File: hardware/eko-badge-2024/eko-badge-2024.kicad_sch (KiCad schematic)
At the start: 34 parts, among them J1 UART, J2 Battery, J3 Conn_02x03_Odd_Even, J4 OLED, J5 Conn_02x03_Odd_Even, J6 Conn_02x03_Odd_Even, P1 USB_C_Plug_USB2.0, Q1 DMG3415U-7, SW1 ON, SW2 LEFT, SW3 UP, SW4 DOWN, SW5 RESET, SW6 BOOT, SW7 RIGTH, U1 ESP32-C6-WROOM-1-N4, U2 AP2112K-3.3

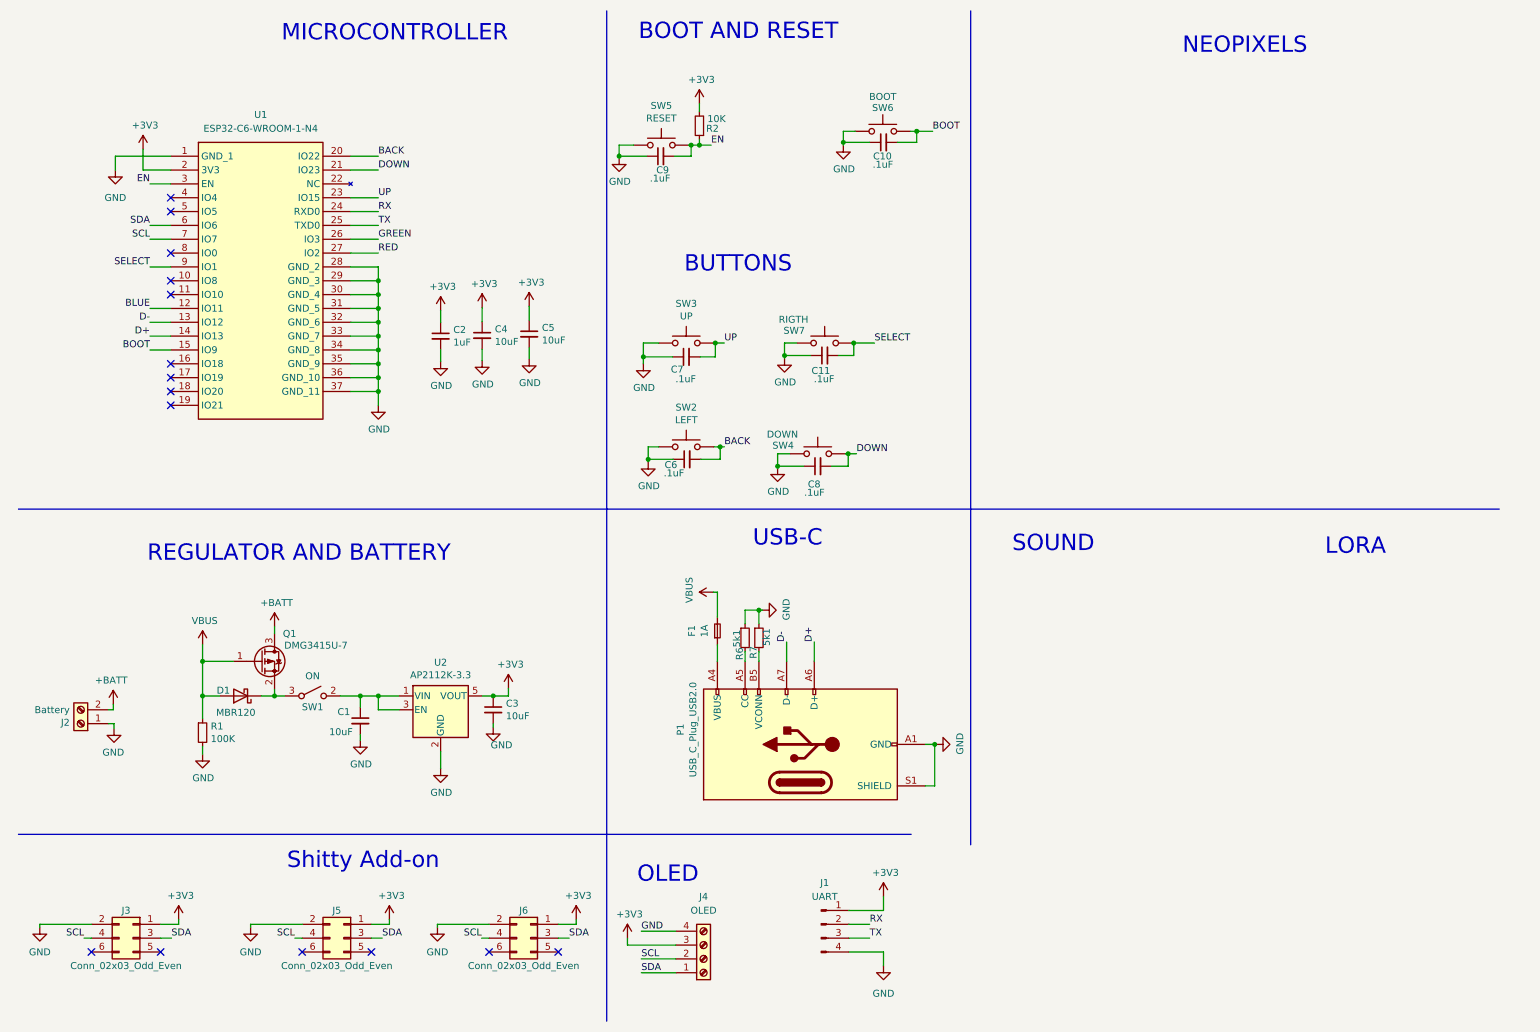
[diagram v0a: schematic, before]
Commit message: feat(Hw):Update_PCB_Added_LoRa_And_Sound_Module
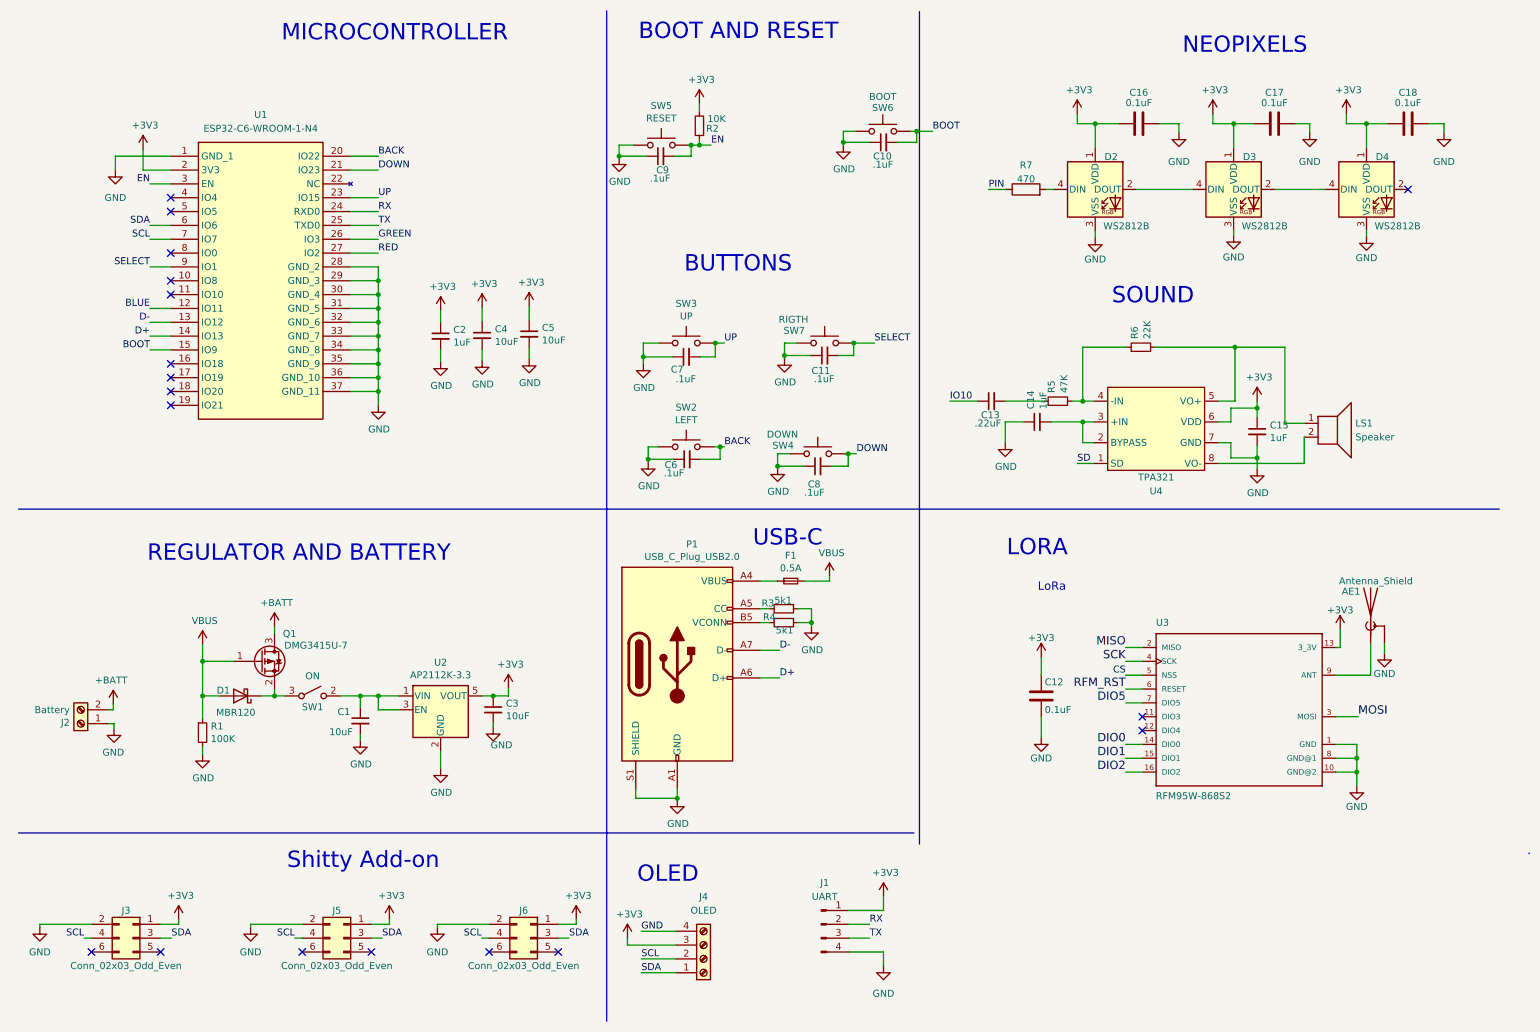
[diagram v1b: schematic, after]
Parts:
- removed R7: 5k1, Resistor_SMD:R_0603_1608Metric, symbol Device:R_Small
- added AE1: Antenna_Shield, agroin:SMA_EDGE, symbol Device:Antenna_Shield
- added C12, C16, C17, C18: 0.1uF, Capacitor_SMD:C_0603_1608Metric, symbol Device:C
- added C13: .22uF, Capacitor_SMD:C_0603_1608Metric, symbol Device:C_Small
- added C14, C15: 1uF, Capacitor_SMD:C_0603_1608Metric, symbol Device:C_Small
- added D2, D3, D4: WS2812B, FootprintsB:LED-SMD_4P-L3.5-W3.5-TL_WS2812B, symbol LED:WS2812B
- added LS1: Speaker, symbol Device:Speaker
- added R3, R4: 5k1, Resistor_SMD:R_0603_1608Metric, symbol Device:R_Small
- added R5: 47K, Resistor_SMD:R_0603_1608Metric, symbol Device:R_Small
- added R7: 470, Resistor_SMD:R_0603_1608Metric, symbol Device:R
- added U3: RFM95W-868S2, RF_Module:HOPERF_RFM9XW_SMD, symbol agroin:RFM95W-868S2
- added U4: TPA321, Package_SO:SOP-8_3.9x4.9mm_P1.27mm, symbol Ekoparty-2024:8002A
- F1: value 1A -> 0.5A; LCSC# C2649564 -> -; manf# MFU0805FF01000P100 -> MFU0805FF00500P100; provedor (none) -> MOUSER
- P1: footprint Footprints:C393939 -> Footprint:C393939; LCSC# C2760486 -> C2987386; manf# (none) -> TYPE-C-31-M-31; provedor (none) -> LCSC
- R6: value 5k1 -> 22K; LCSC# C311919 -> C217281; manf# (none) -> CR-03JL7---10K; provedor (none) -> LCSC
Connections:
- net +3V3: now also C12.1, C15.1, C16.2, C17.2, C18.2, D2.1 (VDD), D3.1 (VDD), D4.1 (VDD), U3.13 (3_3V), U4.6 (VDD)
- net GND: now also AE1.2 (Shield), C12.2, C14.1, C15.2, C16.1, C17.1, C18.1, D2.3 (VSS), D3.3 (VSS), D4.3 (VSS), R3.1, R4.1, U3.1 (GND), U3.10 (GND@2), U3.8 (GND@1), U4.7 (GND); no longer R6.1
- net at R6.2: now also LS1.1, U4.5 (VO+); no longer P1.A5 (CC)
- net at P1.B5 (VCONN): now also R4.2
- new net: C14.2, U4.2 (BYPASS), U4.3 (+IN)
- new net: D2.4 (DIN), R7.2
- new net: R5.2, R6.1, U4.4 (-IN)
- new net: LS1.2, U4.8 (VO-)
- new net: D3.2 (DOUT), D4.4 (DIN)
- new net: D2.2 (DOUT), D3.4 (DIN)
- new net: AE1.1 (A), U3.9 (ANT)
- new net: C13.2, R5.1
- new net: P1.A5 (CC), R3.2
- new net CS: U3.5 (NSS)
- new net DIO0: U3.14 (DIO0)
- new net DIO1: U3.15 (DIO1)
- new net DIO2: U3.16 (DIO2)
- new net DIO5: U3.7 (DIO5)
- new net IO10: C13.1
- new net MISO: U3.2 (MISO)
- new net MOSI: U3.3 (MOSI)
- new net PIN: R7.1
- new net RFM_RST: U3.6 (RESET)
- new net SCK: U3.4 (SCK)
- new net SD: U4.1 (SD)
- no-connect marks 15 -> 18
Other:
- note added: "LoRa"

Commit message: feat(Hw):Added_First_Route
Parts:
- removed J5, J6: Conn_02x03_Odd_Even, Connector_PinSocket_2.54mm:PinSocket_2x03_P2.54mm_Vertical, symbol Connector_Generic:Conn_02x03_Odd_Even
- removed U1: ESP32-C6-WROOM-1-N4, Footprints:ESP32C6WROOM1N4, symbol ESP32-C6-WROOM-1-N4:ESP32-C6-WROOM-1-N4
- added J7: Battery, Eko2024:BH-AA-A1AJ020, symbol Connector:Screw_Terminal_01x02
- added R8: 3.3K, Resistor_SMD:R_0603_1608Metric, symbol Device:R_Small
- added U1: ESP32-C6-WROOM-1-N4, bsides:XCVR_ESP32-C6-WROOM-1-N8, symbol Minino:ESP32-C6-WROOM-1U-N8
- AE1: footprint agroin:SMA_EDGE -> Eko2024:SMA_EDGE
- C1, C3, C4, C5: Proveedor (none) -> JLCPCB; manf# (none) -> GRM188R61E106KA73J; provedor (none) -> LCSC
- C14: value 1uF -> .1uF; LCSC# C15849 -> C478888
- C2: Proveedor (none) -> JLCPCB; manf# (none) -> TMK107BJ105KA8T; provedor (none) -> LCSC
- D1: Proveedor (none) -> JLCPCB; manf# MBR120LSF -> MBR120LSFT1G; provedor (none) -> LCSC
- D2, D3, D4: footprint FootprintsB:LED-SMD_4P-L3.5-W3.5-TL_WS2812B -> LED_SMD:LED_WS2812B-Mini_PLCC4_3.5x3.5mm
- F1: value 0.5A -> 0.75A; LCSC# - -> C1972808; Proveedor (none) -> JLCPCB; manf# MFU0805FF00500P100 -> MFU0805FF00750P100
- J1: footprint Footprints:PinHeader_1x04_P2.54mm_Vertical -> Connector_PinHeader_2.54mm:PinHeader_1x04_P2.54mm_Vertical
- J2: footprint Footprints:BAT-TH_BH-AAA-A1AJ024 -> Eko2024:BH-AA-A1AJ020; LCSC# C5290193 -> C5290181; Proveedor (none) -> JLCPCB y LCSC; manf# - -> (none); provedor (none) -> -
- J3: value Conn_02x03_Odd_Even -> Lentes
- J4: footprint Footprints:Display OLED 128 x32 -> Eko2024:Display OLED 128 x32
- LS1: value Speaker -> 931-SPKM.20.8.A-ND; footprint (none) -> Connector_PinHeader_1.27mm:PinHeader_1x02_P1.27mm_Vertical; manf# (none) -> 931-SPKM.20.8.A-ND; provedor (none) -> Digikey
- P1: footprint Footprint:C393939 -> Eko2024:C393939
- Q1: Proveedor (none) -> JLCPCB; manf# (none) -> DMG3415UQ-7; provedor (none) -> LCSC
- R1: Proveedor (none) -> JLCPCB; manf# (none) -> RC0603DR-07100KL; provedor (none) -> LCSC
- SW1: footprint Footprints:JS102011SAQN -> Eko2024:MSK12C02; LCSC# - -> C431540; Proveedor (none) -> JLCPCB; manf# JS102011SAQN -> (none); provedor (none) -> MOUSER
- U2: LCSC# C150742 -> C51118; Proveedor (none) -> JLCPCB; manf# AP7365-33WG-7 -> AP2112K3.3TRG; provedor (none) -> LCSC
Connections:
- net BOOT: now also U1.15 (IO9)
- net CS: now also U1.16 (IO18)
- net D+: now also U1.14 (IO13)
- net D-: now also U1.13 (IO12)
- net DIO0: now also U1.5 (IO5)
- net DIO1: now also U1.27 (IO2)
- net DIO2: now also U1.4 (IO4)
- net DIO5: now also U1.26 (IO3)
- net DOWN: now also U1.21 (IO23)
- net EN: now also U1.3 (EN)
- net GND: now also J7.1 (Pin_1), U1.1 (GND), U1.28 (GND), U1.29 (GND), U1.30 (GND), U1.31 (GND), U1.32 (GND), U1.33 (GND), U1.34 (GND), U1.35 (GND), U1.36 (GND), U1.37 (GND); no longer J2.1 (Pin_1), J3.2 (Pin_2)
- net PIN: now also U1.11 (IO10)
- net RFM_RST: now also R8.1, U1.10 (IO8)
- net RX: now also U1.24 (RXD0)
- net SCK: now also U1.19 (IO21)
- net SCL: now also U1.7 (IO7); no longer J3.4 (Pin_4)
- net SD: now also U1.8 (IO40)
- net SDA: now also U1.6 (IO6); no longer J3.3 (Pin_3)
- net TX: now also U1.25 (TXD0)
- net UP: now also U1.20 (IO22)
- net VBUS: now also C1.1, U2.1 (VIN), U2.3 (EN); no longer D1.2 (A), Q1.1 (G), R1.1
- net at D1.1 (K), Q1.2 (S): now also SW1.2 (B); no longer SW1.3 (A)
- net +3V3 renamed VOUT
- net VOUT: now also SW1.3 (A), R8.2, U1.2 (3V3); no longer C3.1, J3.1 (Pin_1), U2.5 (VOUT)
- net BACK renamed LEFT
- net LEFT: now also U1.9 (IO1)
- net IO10 renamed IO11
- net IO11: now also U1.12 (IO11)
- net MISO renamed CIPO
- net CIPO: now also U1.18 (IO20)
- net MOSI renamed COPI
- net COPI: now also U1.17 (IO19)
- net SELECT renamed RIGHT
- net RIGHT: now also U1.23 (IO15)
- new net: J2.1 (Pin_1), J7.2 (Pin_2)
- new net: C3.1, D1.2 (A), Q1.1 (G), R1.1, U2.5 (VOUT)
- no-connect marks 18 -> 10
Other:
- moved on the sheet: C10, J3, SW6
